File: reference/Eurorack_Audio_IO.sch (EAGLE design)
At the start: 32 parts, among them J1 EURO_JACK, U1 ES_DAISY_SEED_REV4, U11 TL074, U4 TL074

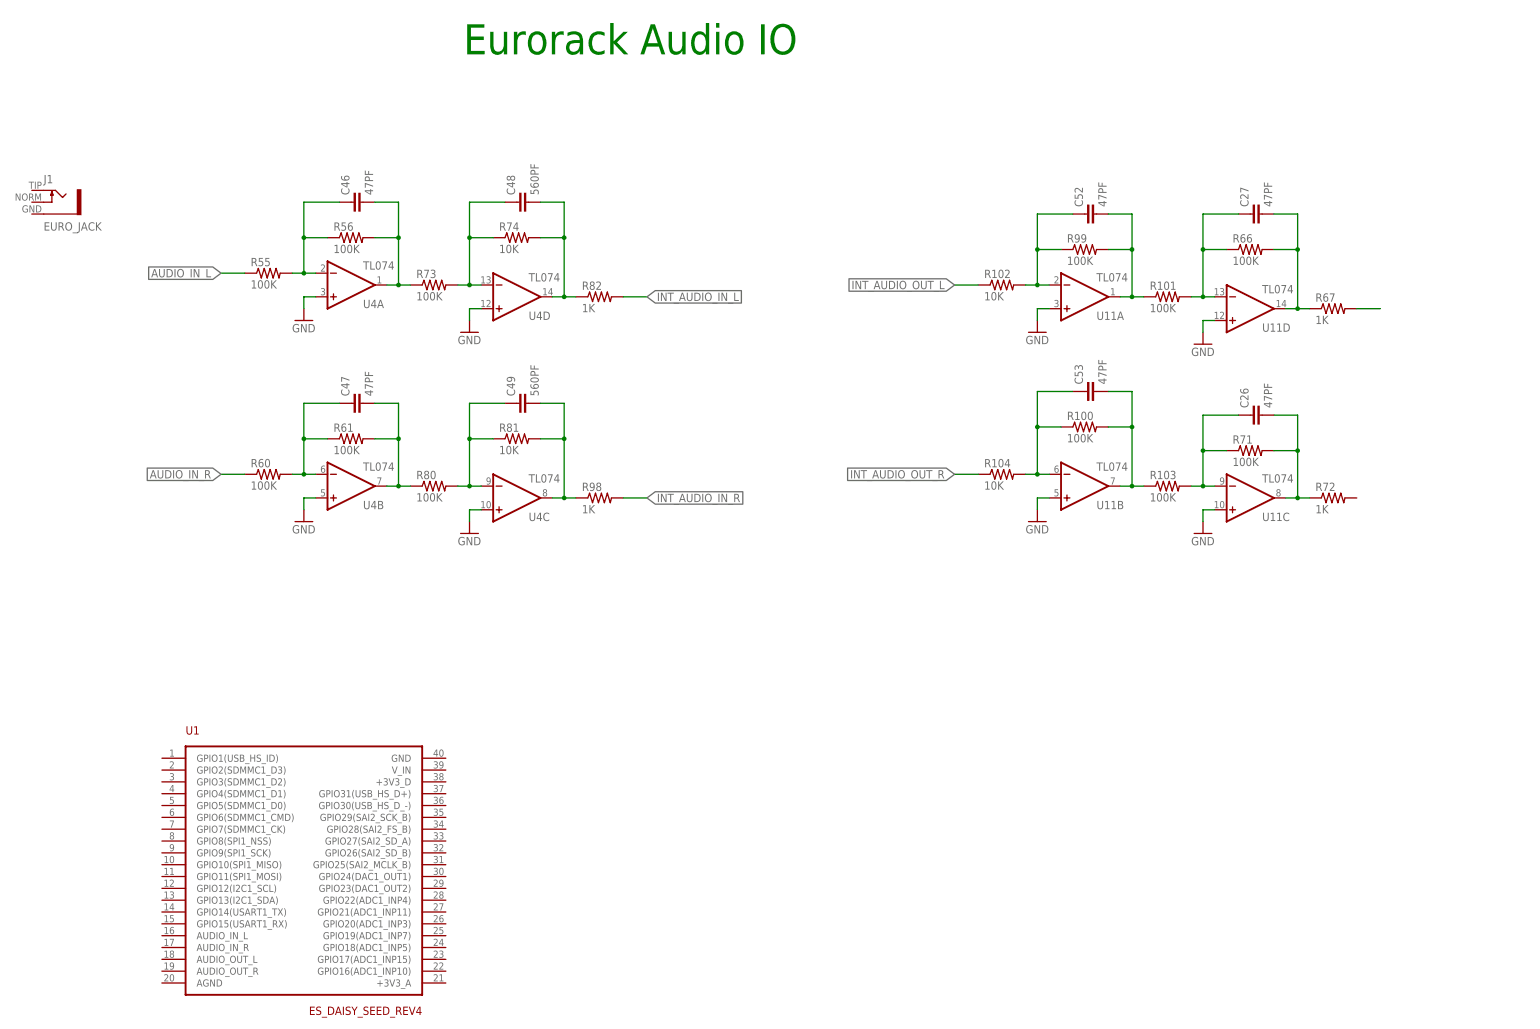
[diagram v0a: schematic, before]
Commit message: finished audio io
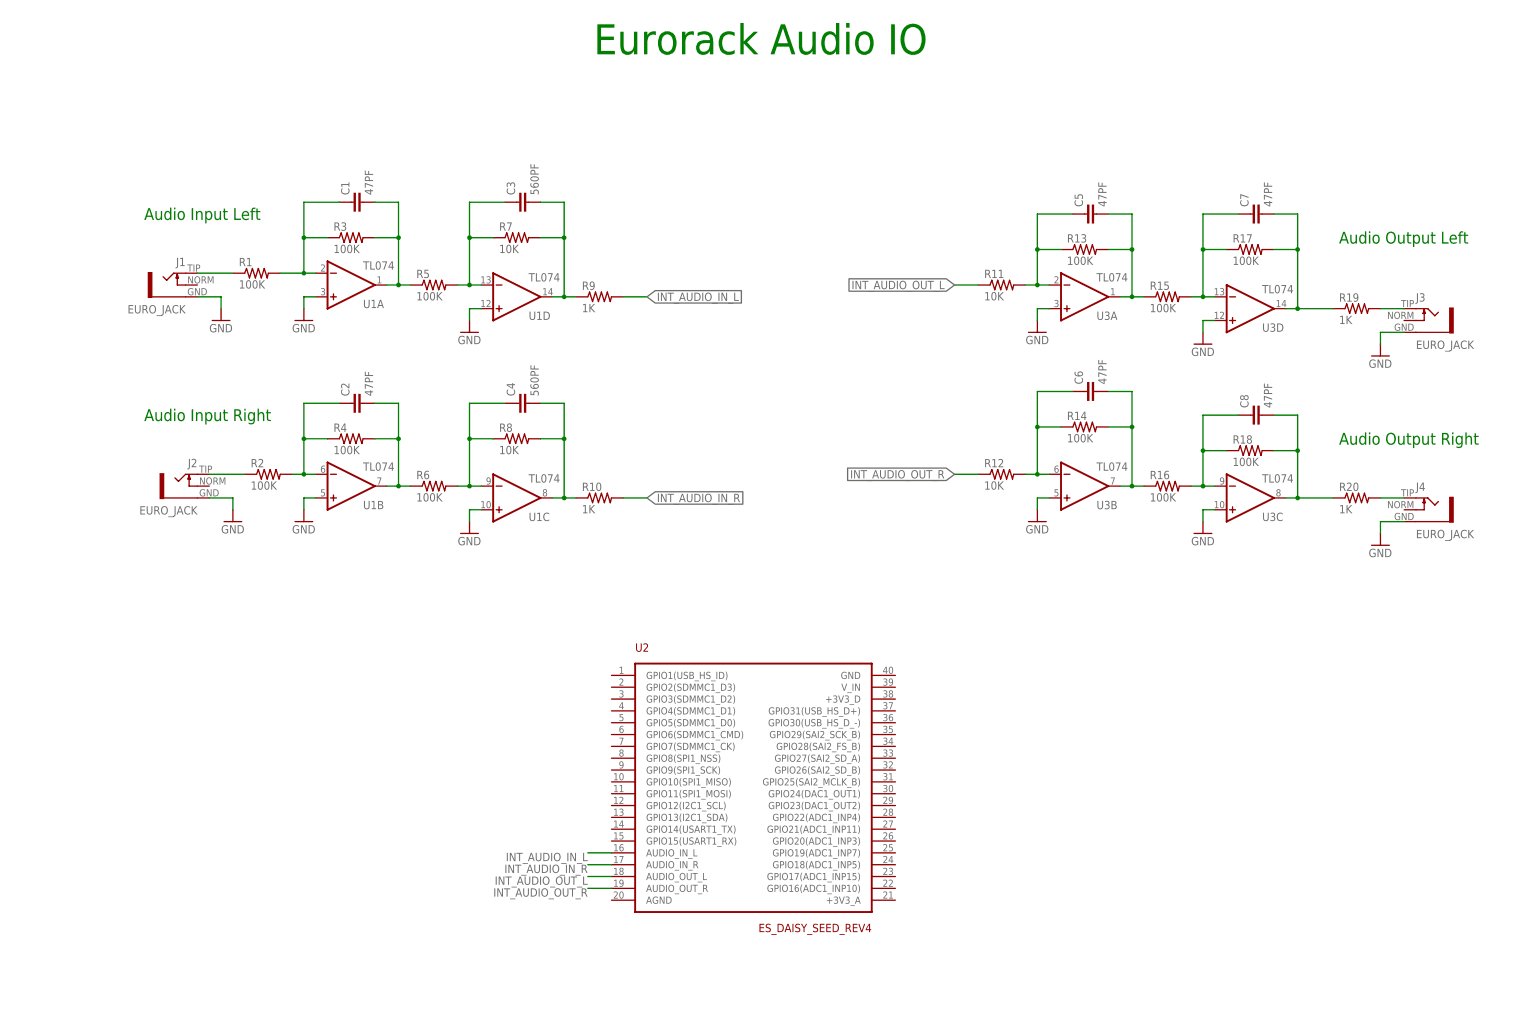
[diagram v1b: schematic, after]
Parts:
- removed R55: 100K, Electrosmith-Passives:R-US_R0603
- removed R67, R72: 1K, Electrosmith-Passives:R-US_R0603
- removed U4: TL074, Electrosmith-IC:TL074_TSSOP-14
- added J2, J3, J4: EURO_JACK, Electrosmith-Interface:EURO_JACK
- added R1: 100K, Electrosmith-Passives:R-US_R0603
- added R19, R20: 1K, Electrosmith-Passives:R-US_R0603
- added U2: ES_DAISY_SEED_REV4, Electrosmith-Boards:ES_DAISY_SEED_REV4
- U1: value ES_DAISY_SEED_REV4 -> TL074; device Electrosmith-Boards:ES_DAISY_SEED_REV4 -> Electrosmith-IC:TL074_TSSOP-14
- renumbered C26 to C8, C27 to C7, C46 to C1, C47 to C2, C48 to C3, C49 to C4, C52 to C5, C53 to C6, R100 to R14, R101 to R15, R102 to R11, R103 to R16, R104 to R12, R56 to R3, R60 to R2, R61 to R4, R66 to R17, R71 to R18, R73 to R5, R74 to R7, R80 to R6, R81 to R8, R82 to R9, R98 to R10, R99 to R13, U11 to U3
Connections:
- removed net AUDIO_IN_R: R2.1
- new net AUDIO_IN_L1: J2.TIP, R2.1
- new net N$2: J4.TIP, R20.2
- net AUDIO_IN_L: now also J1.TIP, R1.1; no longer R55.1
- net GND: now also J1.GND, J2.GND, J3.GND, J4.GND, U1A.+IN, U1B.+IN, U1C.+IN, U1D.+IN; no longer U4A.+IN, U4B.+IN, U4C.+IN, U4D.+IN
- net INT_AUDIO_IN_L: now also U2.AUDIO_IN_L
- net INT_AUDIO_IN_R: now also U2.AUDIO_IN_R
- net INT_AUDIO_OUT_L: now also U2.AUDIO_OUT_L
- net INT_AUDIO_OUT_R: now also U2.AUDIO_OUT_R
- net N$1: now also J3.TIP, R19.2; no longer R67.2
- net N$100: now also U1C.OUT; no longer U4C.OUT
- net N$101: now also U1D.OUT; no longer U4D.OUT
- net N$5: now also U1D.-IN; no longer U4D.-IN
- net N$67: now also R1.2, U1A.-IN; no longer R55.2, U4A.-IN
- net N$69: now also U1A.OUT; no longer U4A.OUT
- net N$70: now also U1B.-IN; no longer U4B.-IN
- net N$71: now also U1B.OUT; no longer U4B.OUT
- net N$82: now also R19.1; no longer R67.1
- net N$85: now also U1C.-IN; no longer U4C.-IN
- net N$88: now also R20.1; no longer R72.1
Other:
- note added: "Audio Input Left"
- note added: "Audio Input Right"
- note added: "Audio Output Left"
- note added: "Audio Output Right"
- moved on the sheet: J1
